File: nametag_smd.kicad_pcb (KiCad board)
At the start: 2 copper layers, 89 x 35 mm, 116 parts, among them IC1 ATTINY13-S, P1 ISP, Q1 2N7002, Q2 2N7002, Q3 2N7002, Q4 2N7002, Q5 2N7002

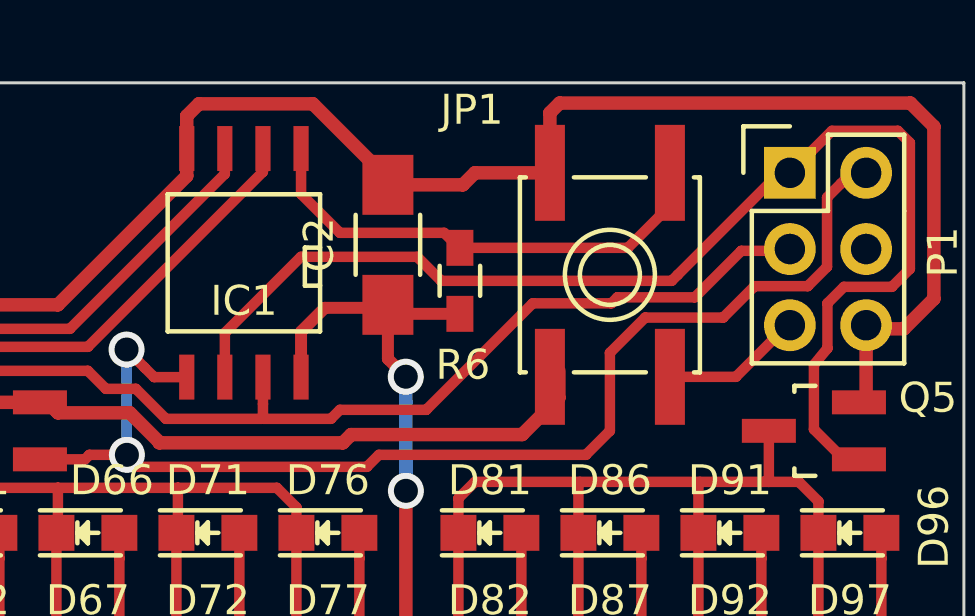
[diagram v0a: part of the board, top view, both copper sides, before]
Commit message: Added missing library components.
Cleaned up a bit the area under the switch to make PCB production easier.
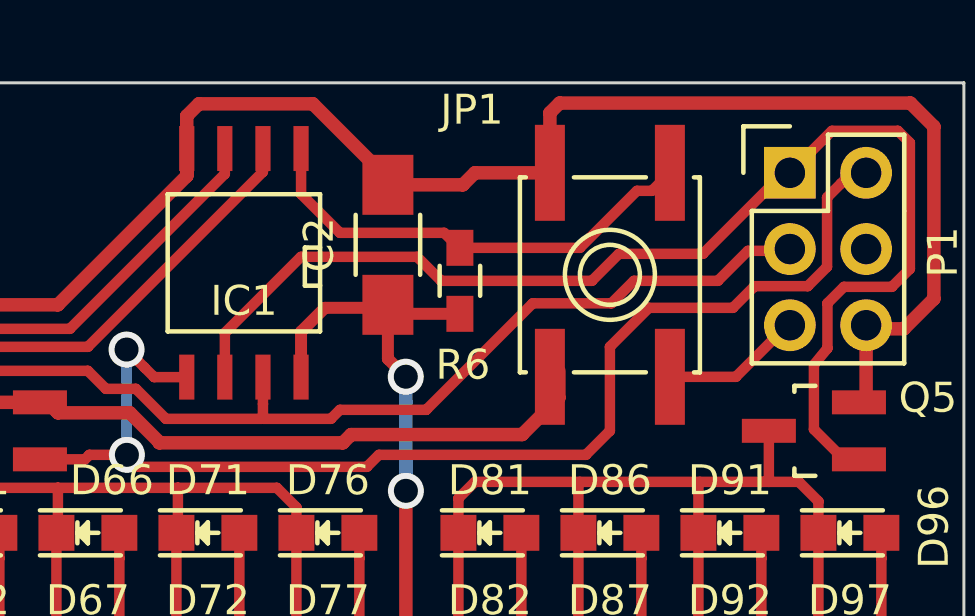
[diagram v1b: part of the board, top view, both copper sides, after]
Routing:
- net GND: track 128.7 -> 129.6 mm
- net /~RESET: track 20.7 -> 20.0 mm
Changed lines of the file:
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@@
     (thickness 1.6)
     (drawings 7)
-    (tracks 545)
+    (tracks 548)
     (zones 0)
     (modules 116)
@@
   (segment (start 131.7 92) (end 130.2 92) (width 0.45) (layer F.Cu) (net 1))
   (segment (start 129.1 92) (end 130.2 92) (width 0.45) (layer F.Cu) (net 1))
+  (segment (start 175.095 61.19) (end 175.095 62.105) (width 0.45) (layer F.Cu) (net 2))
   (segment (start 197.8 66.54) (end 197.8 67.2) (width 0.45) (layer F.Cu) (net 2))
   (segment (start 197.8 67.2) (end 199 67.2) (width 0.45) (layer F.Cu) (net 2))
@@
   (segment (start 186.24902 78) (end 186.24902 82) (width 0.35) (layer F.Cu) (net 12))
   (segment (start 186.24902 74) (end 186.24902 78) (width 0.35) (layer F.Cu) (net 12))
+  (segment (start 191.2 62) (end 190.6 62.6) (width 0.35) (layer F.Cu) (net 13))
+  (segment (start 190.6 62.6) (end 190.1 62.6) (width 0.35) (layer F.Cu) (net 13))
+  (segment (start 190.1 62.6) (end 188.2 64.5) (width 0.35) (layer F.Cu) (net 13))
+  (segment (start 188.2 64.5) (end 184.2 64.5) (width 0.35) (layer F.Cu) (net 13))
   (segment (start 195.26 66.54) (end 195.26 66.94) (width 0.35) (layer F.Cu) (net 13))
   (segment (start 195.26 66.94) (end 193.4 68.8) (width 0.35) (layer F.Cu) (net 13))
@@
   (segment (start 183.674999 64) (end 184.174999 64.5) (width 0.35) (layer F.Cu) (net 13))
   (segment (start 184.174999 64.5) (end 184.2 64.5) (width 0.25) (layer F.Cu) (net 13))
-  (segment (start 191.2 62) (end 190.9 62.3) (width 0.35) (layer F.Cu) (net 13))
-  (segment (start 190.9 62.3) (end 190.9 63.4) (width 0.35) (layer F.Cu) (net 13))
-  (segment (start 190.9 63.4) (end 189.8 64.5) (width 0.35) (layer F.Cu) (net 13))
-  (segment (start 189.8 64.5) (end 184.2 64.5) (width 0.35) (layer F.Cu) (net 13))
+  (segment (start 176.365 69.21) (end 176.365 67.335) (width 0.35) (layer F.Cu) (net 14))
+  (segment (start 176.365 67.335) (end 178.9 64.8) (width 0.35) (layer F.Cu) (net 14))
+  (segment (start 178.9 64.8) (end 182.774998 64.8) (width 0.35) (layer F.Cu) (net 14))
+  (segment (start 182.774998 64.8) (end 183.574998 65.6) (width 0.35) (layer F.Cu) (net 14))
+  (segment (start 189.5 64.7) (end 192.3 64.7) (width 0.35) (layer F.Cu) (net 14))
+  (segment (start 183.574998 65.6) (end 188.6 65.6) (width 0.35) (layer F.Cu) (net 14))
+  (segment (start 188.6 65.6) (end 189.5 64.7) (width 0.35) (layer F.Cu) (net 14))
+  (segment (start 192.3 64.7) (end 195 62) (width 0.35) (layer F.Cu) (net 14))
+  (segment (start 195 62) (end 195.2 62) (width 0.35) (layer F.Cu) (net 14))
   (segment (start 197.50114 71.55) (end 197.00076 71.55) (width 0.35) (layer F.Cu) (net 14))
   (segment (start 197.00076 71.55) (end 196 70.54924) (width 0.35) (layer F.Cu) (net 14))
@@
   (segment (start 196.6 60.6) (end 198.8 60.6) (width 0.35) (layer F.Cu) (net 14))
   (segment (start 198.8 60.6) (end 199.2 61) (width 0.35) (layer F.Cu) (net 14))
-  (segment (start 176.365 69.21) (end 176.365 67.335) (width 0.35) (layer F.Cu) (net 14))
-  (segment (start 176.365 67.335) (end 178.9 64.8) (width 0.35) (layer F.Cu) (net 14))
-  (segment (start 191.46 65.4) (end 195.2 61.66) (width 0.35) (layer F.Cu) (net 14))
-  (segment (start 178.9 64.8) (end 182.774998 64.8) (width 0.35) (layer F.Cu) (net 14))
-  (segment (start 182.774998 64.8) (end 183.574998 65.6) (width 0.35) (layer F.Cu) (net 14))
-  (segment (start 183.574998 65.6) (end 191.26 65.6) (width 0.35) (layer F.Cu) (net 14))
-  (segment (start 191.26 65.6) (end 191.46 65.4) (width 0.35) (layer F.Cu) (net 14))
   (segment (start 195.26 61.46) (end 195.26 61.34) (width 0.35) (layer F.Cu) (net 14))
-  (segment (start 170.20114 71.55) (end 171.7 71.55) (width 0.35) (layer F.Cu) (net 15))
-  (segment (start 173.1 71.4) (end 171.85 71.4) (width 0.35) (layer F.Cu) (net 15))
-  (segment (start 171.85 71.4) (end 171.7 71.55) (width 0.35) (layer F.Cu) (net 15))
-  (segment (start 173.1 71.4) (end 172.95 71.55) (width 0.35) (layer F.Cu) (net 15))
   (segment (start 196.9 62.36) (end 196.438601 62.821399) (width 0.35) (layer F.Cu) (net 15))
-  (segment (start 192.975001 66.824999) (end 190.375001 66.824999) (width 0.35) (layer F.Cu) (net 15))
   (segment (start 196.438601 62.821399) (end 196.438601 65.134529) (width 0.35) (layer F.Cu) (net 15))
   (segment (start 196.438601 65.134529) (end 195.794529 65.778601) (width 0.35) (layer F.Cu) (net 15))
   (segment (start 195.794529 65.778601) (end 194.021399 65.778601) (width 0.35) (layer F.Cu) (net 15))
-  (segment (start 190.375001 66.824999) (end 189.2 68) (width 0.35) (layer F.Cu) (net 15))
-  (segment (start 194.021399 65.778601) (end 192.975001 66.824999) (width 0.35) (layer F.Cu) (net 15))
+  (segment (start 194.021399 65.778601) (end 193.3 66.5) (width 0.35) (layer F.Cu) (net 15))
+  (segment (start 193.3 66.5) (end 190.5 66.5) (width 0.35) (layer F.Cu) (net 15))
+  (segment (start 190.5 66.5) (end 189.2 67.8) (width 0.35) (layer F.Cu) (net 15))
+  (segment (start 181.1 71.8) (end 173.5 71.8) (width 0.35) (layer F.Cu) (net 15))
+  (segment (start 173.5 71.8) (end 173.1 71.4) (width 0.35) (layer F.Cu) (net 15))
+  (segment (start 189.2 67.8) (end 189.2 70.6) (width 0.35) (layer F.Cu) (net 15))
   (segment (start 189.2 70.6) (end 188.4 71.4) (width 0.35) (layer F.Cu) (net 15))
-  (segment (start 189.2 68) (end 189.2 70.6) (width 0.35) (layer F.Cu) (net 15))
   (segment (start 188.4 71.4) (end 181.5 71.4) (width 0.35) (layer F.Cu) (net 15))
   (segment (start 181.5 71.4) (end 181.1 71.8) (width 0.35) (layer F.Cu) (net 15))
-  (segment (start 181.1 71.8) (end 173.5 71.8) (width 0.35) (layer F.Cu) (net 15))
-  (segment (start 173.5 71.8) (end 173.1 71.4) (width 0.35) (layer F.Cu) (net 15))
+  (segment (start 170.20114 71.55) (end 171.7 71.55) (width 0.35) (layer F.Cu) (net 15))
+  (segment (start 173.1 71.4) (end 171.85 71.4) (width 0.35) (layer F.Cu) (net 15))
+  (segment (start 171.85 71.4) (end 171.7 71.55) (width 0.35) (layer F.Cu) (net 15))
+  (segment (start 173.1 71.4) (end 172.95 71.55) (width 0.35) (layer F.Cu) (net 15))
   (segment (start 173.1 71.4) (end 173.1 70.906466) (width 0.35) (layer B.Cu) (net 15))
   (segment (start 173.1 70.906466) (end 173.088339 70.894805) (width 0.35) (layer B.Cu) (net 15))
@@
   (segment (start 197.8 61.46) (end 196.9 62.36) (width 0.35) (layer F.Cu) (net 15))
   (segment (start 196.9 62.36) (end 196.611399 62.648601) (width 0.25) (layer F.Cu) (net 15))
+  (segment (start 195.2 64.2) (end 194.8 64.6) (width 0.35) (layer F.Cu) (net 16))
+  (segment (start 194.8 64.6) (end 193.8 64.6) (width 0.35) (layer F.Cu) (net 16))
+  (segment (start 193.8 64.6) (end 192.8 65.6) (width 0.35) (layer F.Cu) (net 16))
+  (segment (start 190 65.6) (end 189.24999 66.35001) (width 0.35) (layer F.Cu) (net 16))
+  (segment (start 192.8 65.6) (end 190 65.6) (width 0.35) (layer F.Cu) (net 16))
+  (segment (start 189.24999 66.35001) (end 186.627822 66.35001) (width 0.35) (layer F.Cu) (net 16))
+  (segment (start 186.627822 66.35001) (end 183.077832 69.9) (width 0.35) (layer F.Cu) (net 16))
+  (segment (start 183.077832 69.9) (end 180.2 69.9) (width 0.35) (layer F.Cu) (net 16))
+  (segment (start 180.2 69.9) (end 179.9 70.2) (width 0.35) (layer F.Cu) (net 16))
+  (segment (start 179.9 70.2) (end 177.635 70.2) (width 0.35) (layer F.Cu) (net 16))
   (segment (start 177.6 70.2) (end 174.4 70.2) (width 0.35) (layer F.Cu) (net 16))
   (segment (start 163.00152 71.55) (end 162.50114 71.55) (width 0.35) (layer F.Cu) (net 16))
@@
   (segment (start 171.8 68.6) (end 165.95152 68.6) (width 0.35) (layer F.Cu) (net 16))
   (segment (start 165.95152 68.6) (end 163.00152 71.55) (width 0.35) (layer F.Cu) (net 16))
-  (segment (start 195.2 64.2) (end 194.8 64.6) (width 0.35) (layer F.Cu) (net 16))
-  (segment (start 194.8 64.6) (end 193.578686 64.6) (width 0.35) (layer F.Cu) (net 16))
-  (segment (start 192.028676 66.15001) (end 189.44999 66.15001) (width 0.35) (layer F.Cu) (net 16))
-  (segment (start 193.578686 64.6) (end 192.028676 66.15001) (width 0.35) (layer F.Cu) (net 16))
-  (segment (start 189.24999 66.35001) (end 186.627822 66.35001) (width 0.35) (layer F.Cu) (net 16))
-  (segment (start 189.44999 66.15001) (end 189.24999 66.35001) (width 0.35) (layer F.Cu) (net 16))
-  (segment (start 186.627822 66.35001) (end 183.077832 69.9) (width 0.35) (layer F.Cu) (net 16))
-  (segment (start 183.077832 69.9) (end 180.2 69.9) (width 0.35) (layer F.Cu) (net 16))
-  (segment (start 180.2 69.9) (end 179.9 70.2) (width 0.35) (layer F.Cu) (net 16))
-  (segment (start 179.9 70.2) (end 177.635 70.2) (width 0.35) (layer F.Cu) (net 16))
   (segment (start 177.635 69.706) (end 177.635 70.165) (width 0.35) (layer F.Cu) (net 16))
   (segment (start 177.635 70.165) (end 177.6 70.2) (width 0.25) (layer F.Cu) (net 16))

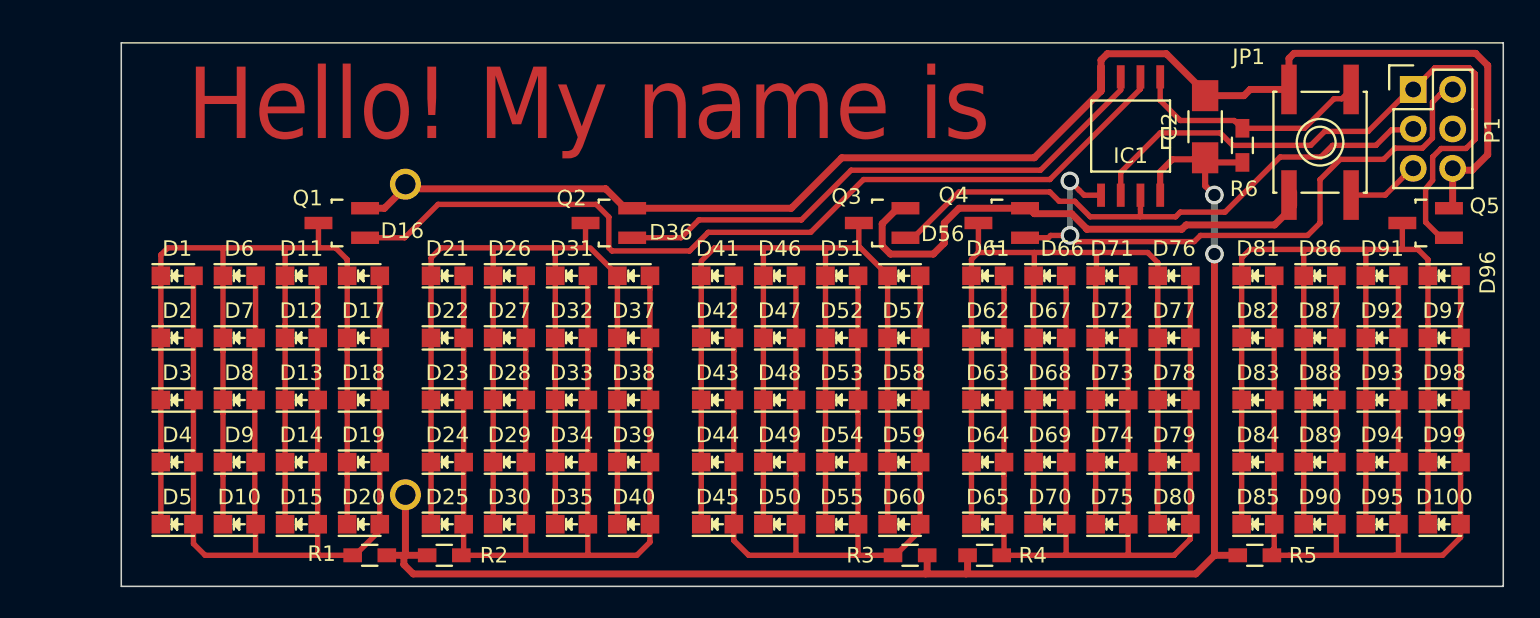
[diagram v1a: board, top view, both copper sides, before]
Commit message: Changed the package variant of the ATTINY13 to SO-8 narrow (ATTINY13-SS) because it is cheaper.
Fixed wrong ISP pinning.

Cleaned up the older thiner pcb tracks.
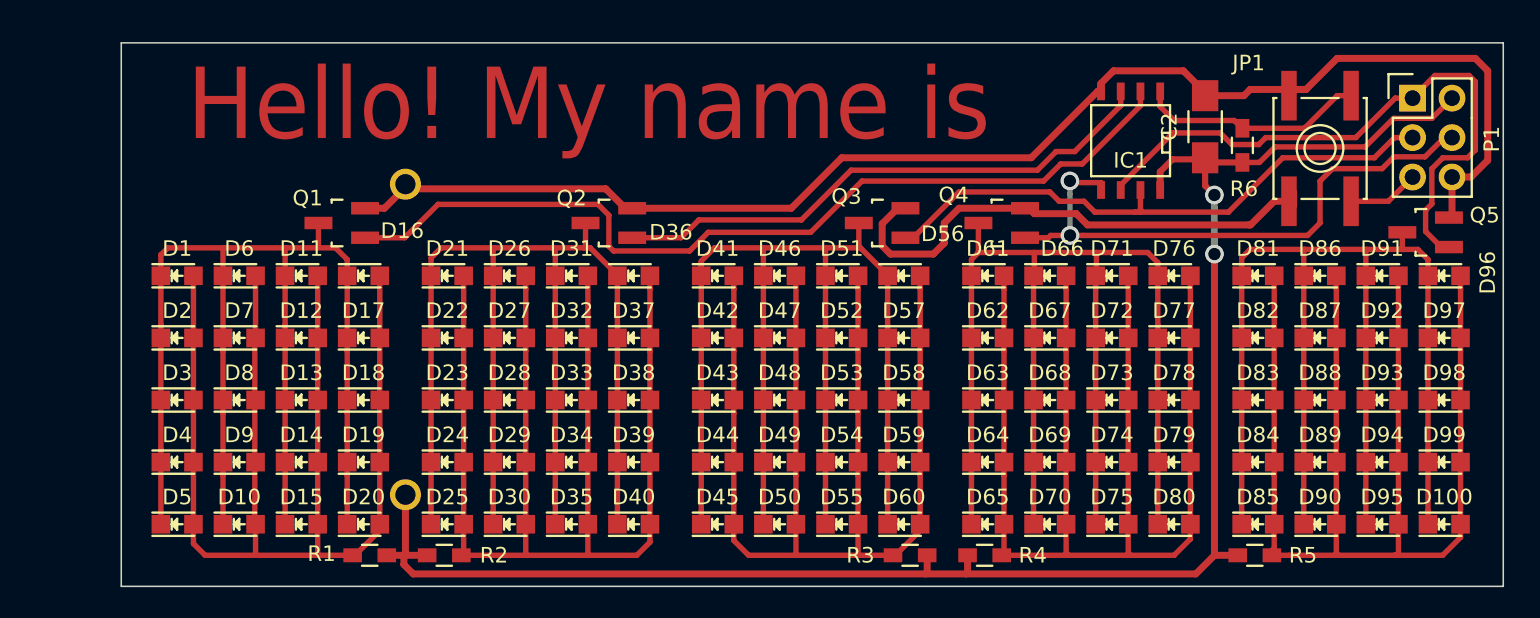
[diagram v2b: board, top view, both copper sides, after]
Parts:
- IC1: value ATTINY13-S -> ATTINY13-SS; footprint nametag:SOIC-8-N_HandSoldering -> SMD_Packages:SOIC-8-N
- moved Q5 0.60 mm to (196.0, 71.2)
- moved P1 0.56 mm to (195.2, 62.6)
- moved JP1 0.40 mm to (189.2, 65.8)
- moved IC1 0.30 mm to (177.0, 65.3)
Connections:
- P1 pad 2: /DIGIT3 -> VCC
- P1 pad 4: Net-(P1-Pad4) -> /DIGIT3
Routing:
- net VCC: track 100.5 -> 115.0 mm
- net GND: track 129.6 -> 125.7 mm
- net /DIGIT3: track 41.6 -> 38.3 mm
- net /DIGIT4: track 41.8 -> 40.9 mm
- net /~RESET: track 20.0 -> 19.3 mm
- net Net-(D100-Pad1): track 83.8 -> 83.2 mm
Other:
- rule trace_min: 0.2 -> 0.35
